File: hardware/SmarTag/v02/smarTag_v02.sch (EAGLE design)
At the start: 17 parts, among them U1 ADXL362

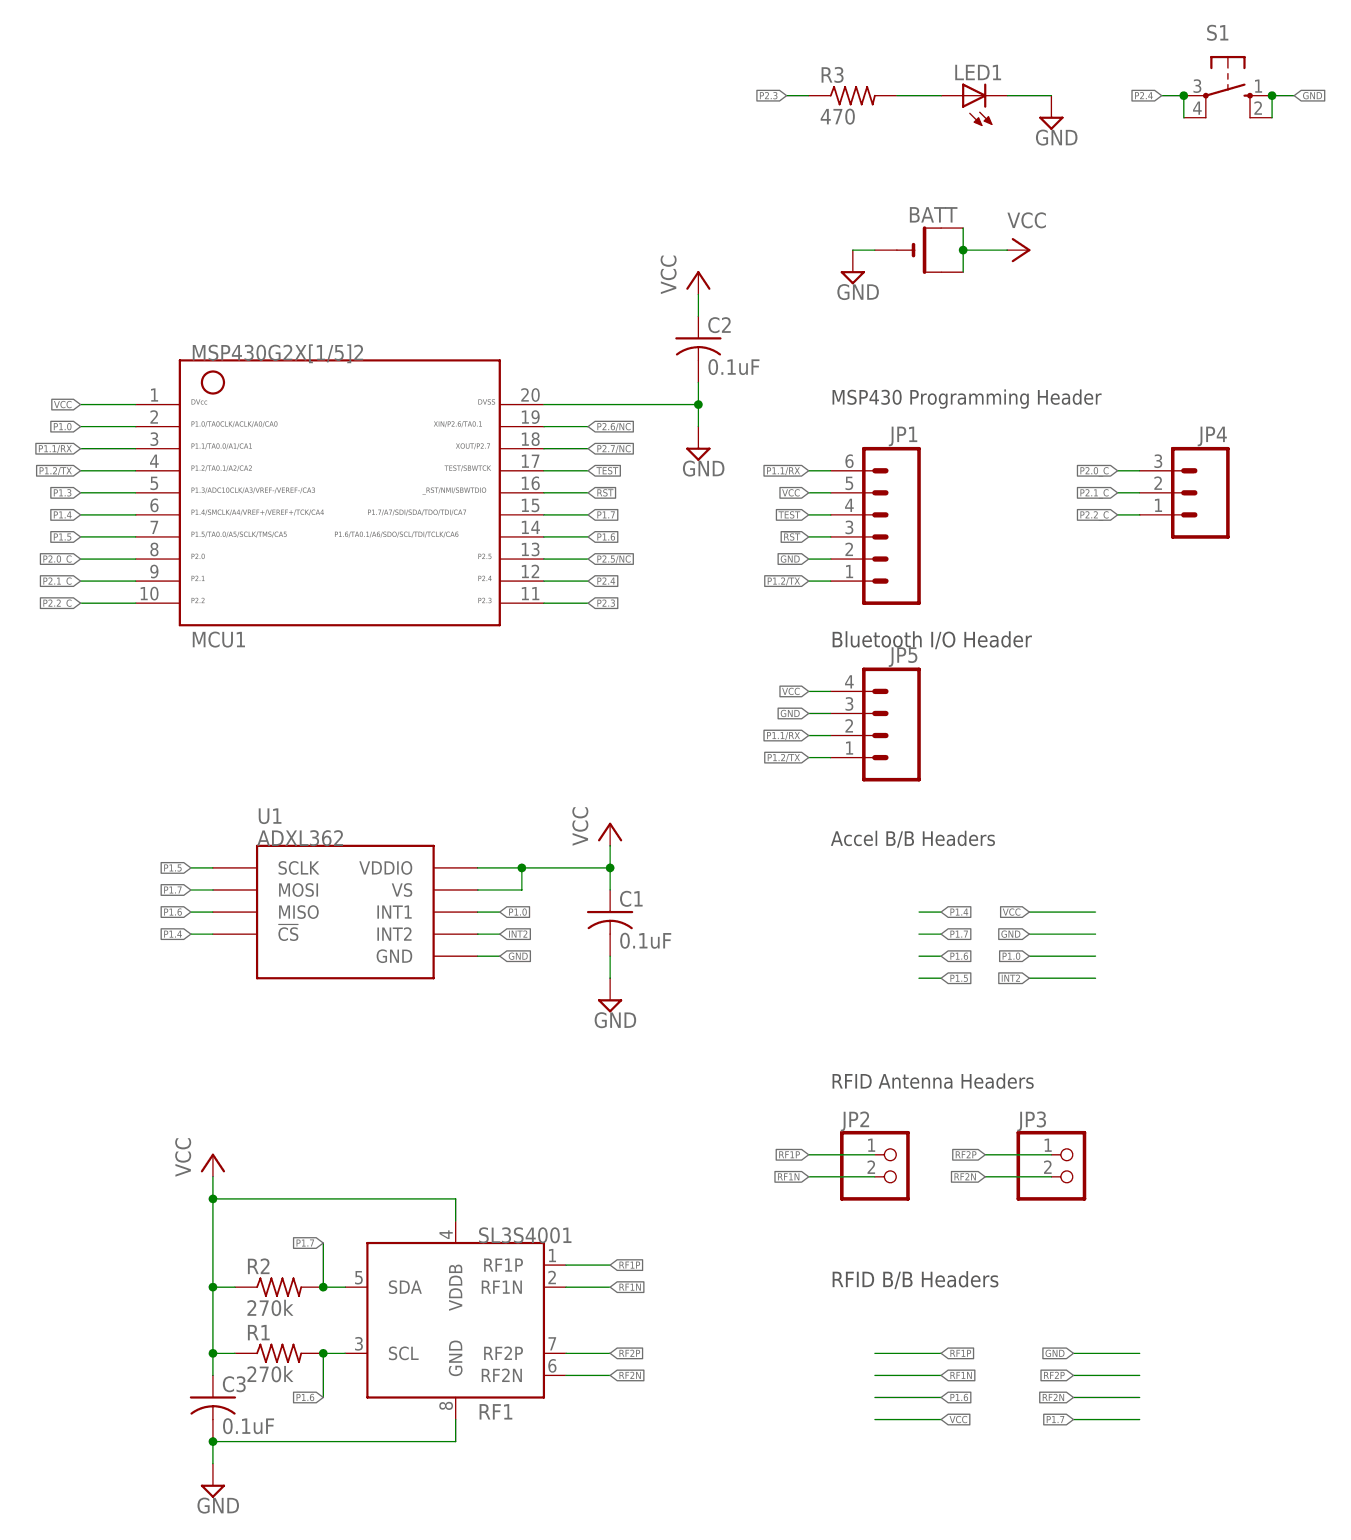
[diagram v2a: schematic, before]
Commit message: hw: Add v02 board.
A complete rework of the board. Includes a new SMD hard switch, no extraneous breakout board headers, and a much smaller overall profile.
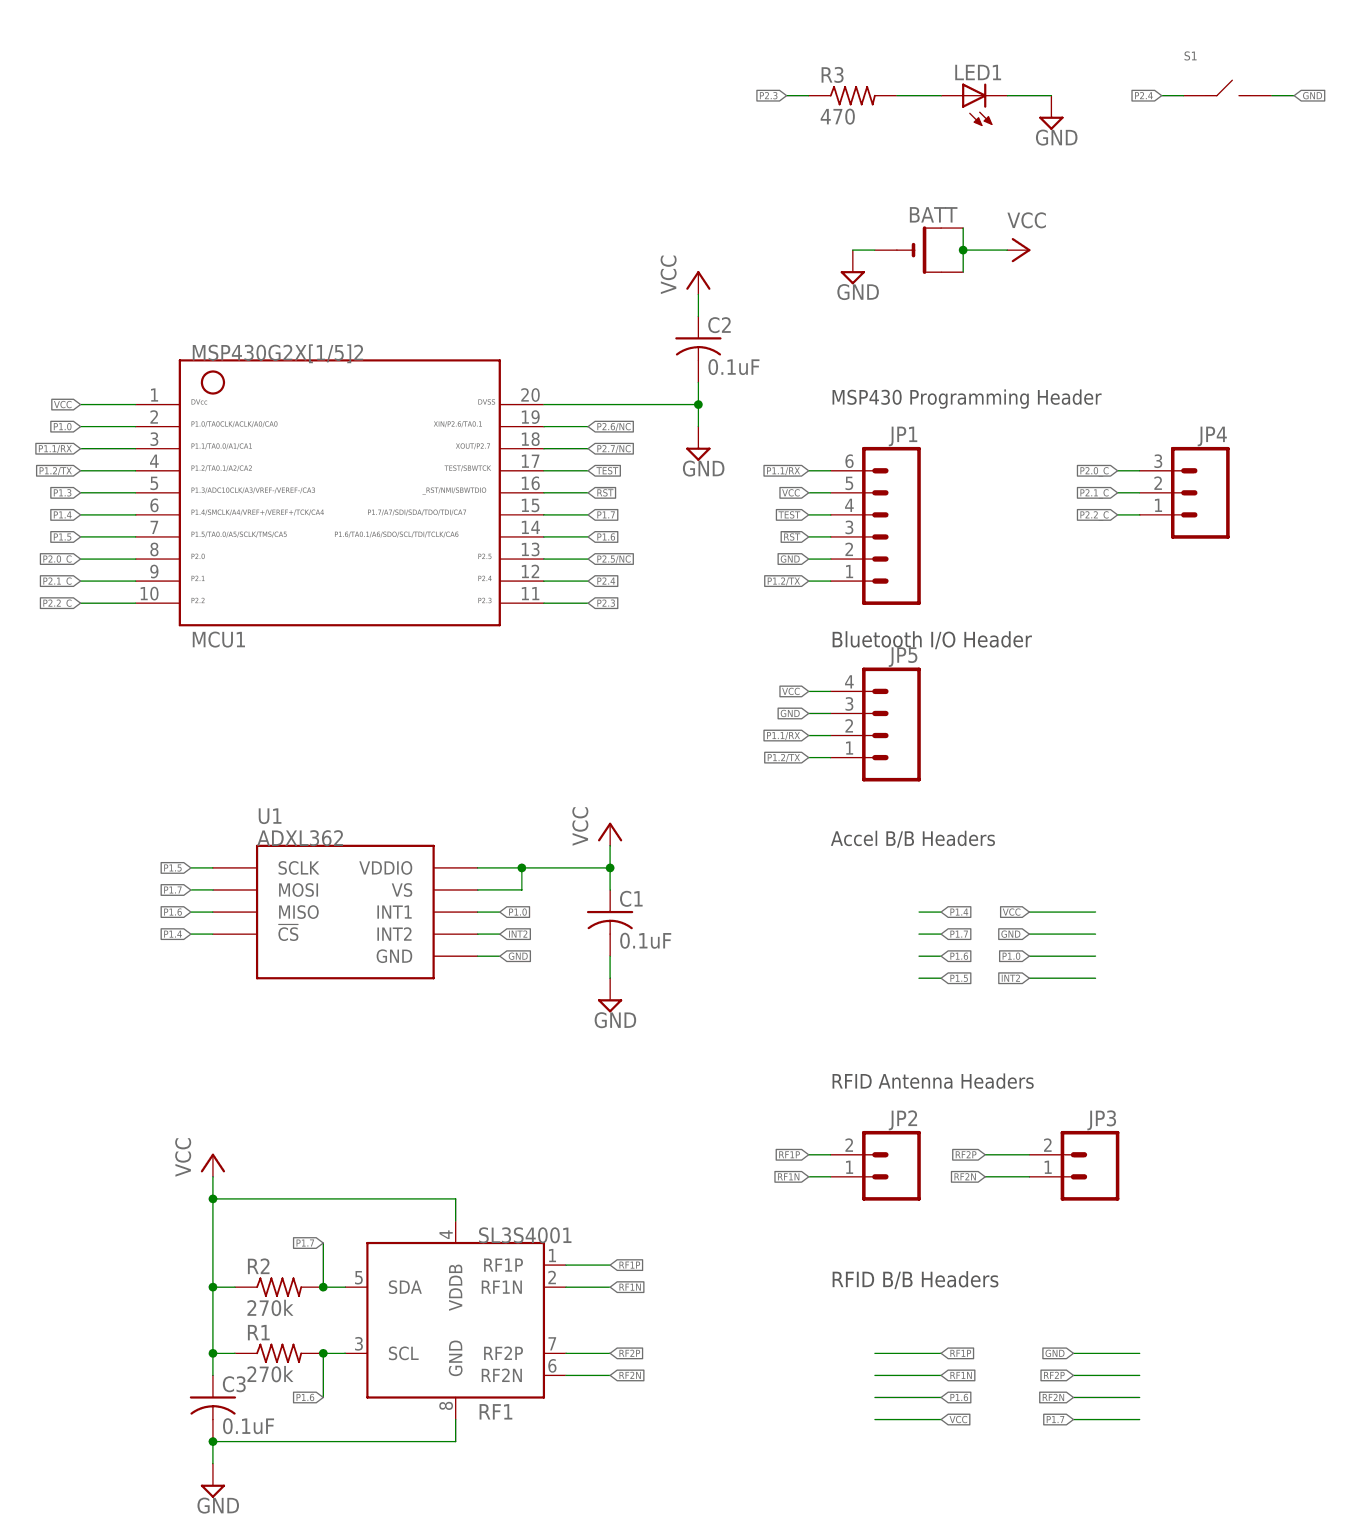
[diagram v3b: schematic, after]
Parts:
- JP2, JP3: device pinhead:PINHD-1X2 -> SparkFun-Connectors:M02LOCK
- S1: device switch-omron:10-XX -> PP_Electromechanical:SPST_B3FS-1000
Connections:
- net GND: now also S1.B; no longer S1.S, S1.S1
- net P2.4: now also S1.A; no longer S1.P, S1.P1
- net RF1N: now also JP2.1; no longer JP2.2
- net RF1P: now also JP2.2; no longer JP2.1
- net RF2N: now also JP3.1; no longer JP3.2
- net RF2P: now also JP3.2; no longer JP3.1
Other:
- moved on the sheet: JP3
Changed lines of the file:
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@@
 <part name="R1" library="rcl" deviceset="R-US_" device="R0805" value="270k"/>
 <part name="SUPPLY3" library="supply2" deviceset="GND" device=""/>
-<part name="JP2" library="pinhead" deviceset="PINHD-1X2" device=""/>
-<part name="JP3" library="pinhead" deviceset="PINHD-1X2" device=""/>
 <part name="U1" library="SparkFun-Sensors" deviceset="ADXL362" device="" value="ADXL362"/>
 <part name="P+3" library="supply1" deviceset="VCC" device=""/>
@@
 <part name="JP1" library="SparkFun-Connectors" deviceset="M06" device="LOCK"/>
 <part name="JP4" library="SparkFun-Connectors" deviceset="M03" device="LOCK"/>
-<part name="S1" library="switch-omron" deviceset="10-XX" device=""/>
 <part name="JP5" library="SparkFun-Connectors" deviceset="M04" device="LOCK"/>
+<part name="JP2" library="SparkFun-Connectors" deviceset="M02" device="LOCK"/>
+<part name="JP3" library="SparkFun-Connectors" deviceset="M02" device="LOCK"/>
+<part name="S1" library="PP_Electromechanical" deviceset="SPST" device="_B3FS-1000"/>
 </parts>
 <sheets>
@@
 <instance part="R1" gate="G$1" x="53.34" y="35.56"/>
 <instance part="SUPPLY3" gate="GND" x="45.72" y="20.32"/>
-<instance part="JP2" gate="G$1" x="124.46" y="55.88"/>
-<instance part="JP3" gate="G$1" x="144.78" y="55.88"/>
 <instance part="U1" gate="G$1" x="60.96" y="86.36"/>
 <instance part="P+3" gate="VCC" x="91.44" y="96.52"/>
@@
 <instance part="JP1" gate="G$1" x="121.92" y="129.54" rot="MR0"/>
 <instance part="JP4" gate="G$1" x="160.02" y="134.62" rot="MR0"/>
-<instance part="S1" gate="1" x="162.56" y="180.34" rot="R270"/>
 <instance part="JP5" gate="G$1" x="121.92" y="106.68" rot="MR0"/>
+<instance part="JP2" gate="G$1" x="124.46" y="55.88" rot="MR0"/>
+<instance part="JP3" gate="G$1" x="147.32" y="55.88" rot="MR0"/>
+<instance part="S1" gate="G$1" x="162.56" y="180.34"/>
 </instances>
 <busses>
@@
 </segment>
 <segment>
-<pinref part="S1" gate="1" pin="P"/>
-<pinref part="S1" gate="1" pin="P1"/>
-<wire x1="157.48" y1="180.34" x2="157.48" y2="177.8" width="0.1524" layer="91"/>
 <wire x1="157.48" y1="180.34" x2="154.94" y2="180.34" width="0.1524" layer="91"/>
-<junction x="157.48" y="180.34"/>
 <label x="154.94" y="180.34" size="0.8128" layer="91" rot="R180" xref="yes"/>
+<pinref part="S1" gate="G$1" pin="A"/>
 </segment>
 </net>
@@
 </segment>
 <segment>
-<pinref part="S1" gate="1" pin="S"/>
-<pinref part="S1" gate="1" pin="S1"/>
-<wire x1="167.64" y1="180.34" x2="167.64" y2="177.8" width="0.1524" layer="91"/>
 <wire x1="167.64" y1="180.34" x2="170.18" y2="180.34" width="0.1524" layer="91"/>
-<junction x="167.64" y="180.34"/>
 <label x="170.18" y="180.34" size="0.8128" layer="91" xref="yes"/>
+<pinref part="S1" gate="G$1" pin="B"/>
 </segment>
 <segment>
@@
 </segment>
 <segment>
-<pinref part="JP2" gate="G$1" pin="1"/>
-<wire x1="121.92" y1="58.42" x2="114.3" y2="58.42" width="0.1524" layer="91"/>
+<wire x1="116.84" y1="58.42" x2="114.3" y2="58.42" width="0.1524" layer="91"/>
 <label x="114.3" y="58.42" size="0.8128" layer="91" rot="MR0" xref="yes"/>
+<pinref part="JP2" gate="G$1" pin="2"/>
 </segment>
 <segment>
@@
 </segment>
 <segment>
-<pinref part="JP2" gate="G$1" pin="2"/>
-<wire x1="121.92" y1="55.88" x2="114.3" y2="55.88" width="0.1524" layer="91"/>
+<wire x1="116.84" y1="55.88" x2="114.3" y2="55.88" width="0.1524" layer="91"/>
 <label x="114.3" y="55.88" size="0.8128" layer="91" rot="MR0" xref="yes"/>
+<pinref part="JP2" gate="G$1" pin="1"/>
 </segment>
 <segment>
@@
 </segment>
 <segment>
-<pinref part="JP3" gate="G$1" pin="2"/>
-<wire x1="142.24" y1="55.88" x2="134.62" y2="55.88" width="0.1524" layer="91"/>
+<wire x1="139.7" y1="55.88" x2="134.62" y2="55.88" width="0.1524" layer="91"/>
 <label x="134.62" y="55.88" size="0.8128" layer="91" rot="MR0" xref="yes"/>
+<pinref part="JP3" gate="G$1" pin="1"/>
 </segment>
 <segment>
@@
 </segment>
 <segment>
-<pinref part="JP3" gate="G$1" pin="1"/>
-<wire x1="142.24" y1="58.42" x2="134.62" y2="58.42" width="0.1524" layer="91"/>
+<wire x1="139.7" y1="58.42" x2="134.62" y2="58.42" width="0.1524" layer="91"/>
 <label x="134.62" y="58.42" size="0.8128" layer="91" rot="MR0" xref="yes"/>
-</segment>
-<segment>
+<pinref part="JP3" gate="G$1" pin="2"/>
+</segment>
+<segment>

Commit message: hw: Update board w/ 1.27mm JP1
This new programming header allows for direct connection with an MSP430
Launchpad for programming and debugging.
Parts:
- JP1: device SparkFun-Connectors:M06LOCK -> SparkFun-Connectors:M061.27MM
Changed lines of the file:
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@@
 <grid distance="0.1" unitdist="inch" unit="inch" style="lines" multiple="1" display="no" altdistance="0.01" altunitdist="inch" altunit="inch"/>
 <layers>
-<layer number="1" name="Top" color="4" fill="1" visible="no" active="no"/>
-<layer number="16" name="Bottom" color="1" fill="1" visible="no" active="no"/>
-<layer number="17" name="Pads" color="2" fill="1" visible="no" active="no"/>
-<layer number="18" name="Vias" color="2" fill="1" visible="no" active="no"/>
-<layer number="19" name="Unrouted" color="6" fill="1" visible="no" active="no"/>
-<layer number="20" name="Dimension" color="15" fill="1" visible="no" active="no"/>
-<layer number="21" name="tPlace" color="7" fill="1" visible="no" active="no"/>
-<layer number="22" name="bPlace" color="7" fill="1" visible="no" active="no"/>
-<layer number="23" name="tOrigins" color="15" fill="1" visible="no" active="no"/>
-<layer number="24" name="bOrigins" color="15" fill="1" visible="no" active="no"/>
-<layer number="25" name="tNames" color="7" fill="1" visible="no" active="no"/>
-<layer number="26" name="bNames" color="7" fill="1" visible="no" active="no"/>
-<layer number="27" name="tValues" color="7" fill="1" visible="no" active="no"/>
-<layer number="28" name="bValues" color="7" fill="1" visible="no" active="no"/>
+<layer number="1" name="Top" color="4" fill="1" visible="yes" active="no"/>
+<layer number="16" name="Bottom" color="1" fill="1" visible="yes" active="no"/>
+<layer number="17" name="Pads" color="2" fill="1" visible="yes" active="no"/>
+<layer number="18" name="Vias" color="2" fill="1" visible="yes" active="no"/>
+<layer number="19" name="Unrouted" color="6" fill="1" visible="yes" active="no"/>
+<layer number="20" name="Dimension" color="15" fill="1" visible="yes" active="no"/>
+<layer number="21" name="tPlace" color="7" fill="1" visible="yes" active="no"/>
+<layer number="22" name="bPlace" color="7" fill="1" visible="yes" active="no"/>
+<layer number="23" name="tOrigins" color="15" fill="1" visible="yes" active="no"/>
+<layer number="24" name="bOrigins" color="15" fill="1" visible="yes" active="no"/>
+<layer number="25" name="tNames" color="7" fill="1" visible="yes" active="no"/>
+<layer number="26" name="bNames" color="7" fill="1" visible="yes" active="no"/>
+<layer number="27" name="tValues" color="7" fill="1" visible="yes" active="no"/>
+<layer number="28" name="bValues" color="7" fill="1" visible="yes" active="no"/>
 <layer number="29" name="tStop" color="7" fill="3" visible="no" active="no"/>
 <layer number="30" name="bStop" color="7" fill="6" visible="no" active="no"/>
@@
 <layer number="35" name="tGlue" color="7" fill="4" visible="no" active="no"/>
 <layer number="36" name="bGlue" color="7" fill="5" visible="no" active="no"/>
-<layer number="37" name="tTest" color="7" fill="1" visible="no" active="no"/>
-<layer number="38" name="bTest" color="7" fill="1" visible="no" active="no"/>
+<layer number="37" name="tTest" color="7" fill="1" visible="yes" active="no"/>
+<layer number="38" name="bTest" color="7" fill="1" visible="yes" active="no"/>
 <layer number="39" name="tKeepout" color="4" fill="11" visible="no" active="no"/>
 <layer number="40" name="bKeepout" color="1" fill="11" visible="no" active="no"/>
@@
 <layer number="44" name="Drills" color="7" fill="1" visible="no" active="no"/>
 <layer number="45" name="Holes" color="7" fill="1" visible="no" active="no"/>
-<layer number="46" name="Milling" color="3" fill="1" visible="no" active="no"/>
-<layer number="47" name="Measures" color="7" fill="1" visible="no" active="no"/>
-<layer number="48" name="Document" color="7" fill="1" visible="no" active="no"/>
-<layer number="49" name="Reference" color="7" fill="1" visible="no" active="no"/>
-<layer number="50" name="dxf" color="7" fill="1" visible="no" active="no"/>
-<layer number="51" name="tDocu" color="7" fill="1" visible="no" active="no"/>
-<layer number="52" name="bDocu" color="7" fill="1" visible="no" active="no"/>
-<layer number="53" name="tGND_GNDA" color="7" fill="9" visible="no" active="no"/>
-<layer number="54" name="bGND_GNDA" color="1" fill="9" visible="no" active="no"/>
-<layer number="56" name="wert" color="7" fill="1" visible="no" active="no"/>
-<layer number="57" name="tCAD" color="7" fill="1" visible="no" active="no"/>
-<layer number="59" name="tCarbon" color="7" fill="1" visible="no" active="no"/>
-<layer number="60" name="bCarbon" color="7" fill="1" visible="no" active="no"/>
+<layer number="46" name="Milling" color="3" fill="1" visible="yes" active="no"/>
+<layer number="47" name="Measures" color="7" fill="1" visible="yes" active="no"/>
+<layer number="48" name="Document" color="7" fill="1" visible="yes" active="no"/>
+<layer number="49" name="Reference" color="7" fill="1" visible="yes" active="no"/>
+<layer number="50" name="dxf" color="7" fill="1" visible="yes" active="no"/>
+<layer number="51" name="tDocu" color="7" fill="1" visible="yes" active="no"/>
+<layer number="52" name="bDocu" color="7" fill="1" visible="yes" active="no"/>
+<layer number="53" name="tGND_GNDA" color="7" fill="9" visible="yes" active="no"/>
+<layer number="54" name="bGND_GNDA" color="1" fill="9" visible="yes" active="no"/>
+<layer number="56" name="wert" color="7" fill="1" visible="yes" active="no"/>
+<layer number="57" name="tCAD" color="7" fill="1" visible="yes" active="no"/>
+<layer number="59" name="tCarbon" color="7" fill="1" visible="yes" active="no"/>
+<layer number="60" name="bCarbon" color="7" fill="1" visible="yes" active="no"/>
 <layer number="90" name="Modules" color="5" fill="1" visible="yes" active="yes"/>
 <layer number="91" name="Nets" color="2" fill="1" visible="yes" active="yes"/>
@@
 <part name="R3" library="rcl" deviceset="R-US_" device="R0805" value="470"/>
 <part name="SUPPLY5" library="supply2" deviceset="GND" device=""/>
-<part name="JP1" library="SparkFun-Connectors" deviceset="M06" device="LOCK"/>
+<part name="JP1" library="SparkFun-Connectors" deviceset="M06" device="1.27MM"/>
 <part name="JP4" library="SparkFun-Connectors" deviceset="M03" device="LOCK"/>
 <part name="JP5" library="SparkFun-Connectors" deviceset="M04" device="LOCK"/>
